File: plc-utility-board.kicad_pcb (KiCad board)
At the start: 2 copper layers, 116 parts, among them J1 Screw_Terminal_01x02, J10 Screw_Terminal_01x03, J11 Screw_Terminal_01x02, J12 Screw_Terminal_01x04, J2 Screw_Terminal_01x08, J3 Screw_Terminal_01x04, J4 Screw_Terminal_01x08, J5 Screw_Terminal_01x04, J6 Conn_01x03_Male, J7 Conn_01x03_Male, J8 Screw_Terminal_01x03, J9 Screw_Terminal_01x02, Q1 2N7002, Q10 2N7002, Q11 2N7002, Q12 2N7002, Q13 FDV304, Q14 2N7002, Q15 2N7002, Q16 2N7002, Q2 2N7002, Q3 Q_PMOS_GSD, Q4 Q_PMOS_GSD, Q5 2N7002, Q6 2N7002, Q7 Q_PMOS_GSD, Q8 Q_PMOS_GSD, Q9 FDV304, SW1 SW_Push, SW2 SW_Push, SW3 SW_Push, SW4 SW_Push, SW5 SW_Push, SW6 SW_Push, U1 L78L33_SOT89, U2 DRV8840, U3 DRV8840

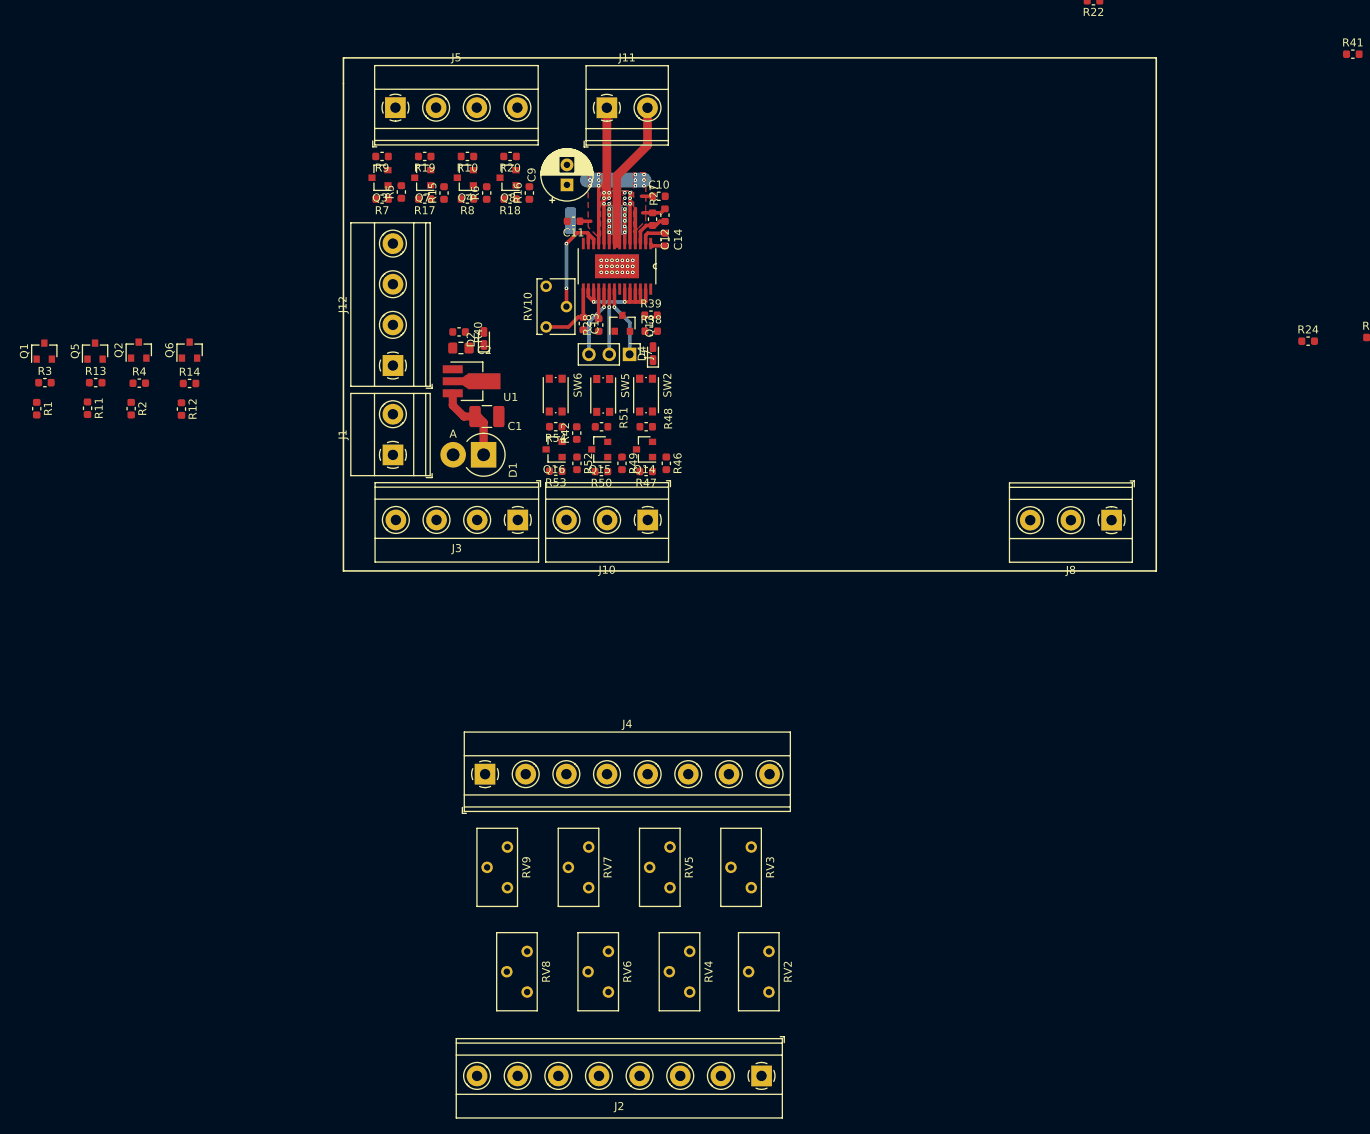
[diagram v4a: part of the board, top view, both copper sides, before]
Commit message: Re-placed components of 3.3->24V converter. Improvement placement of Motor Controller components
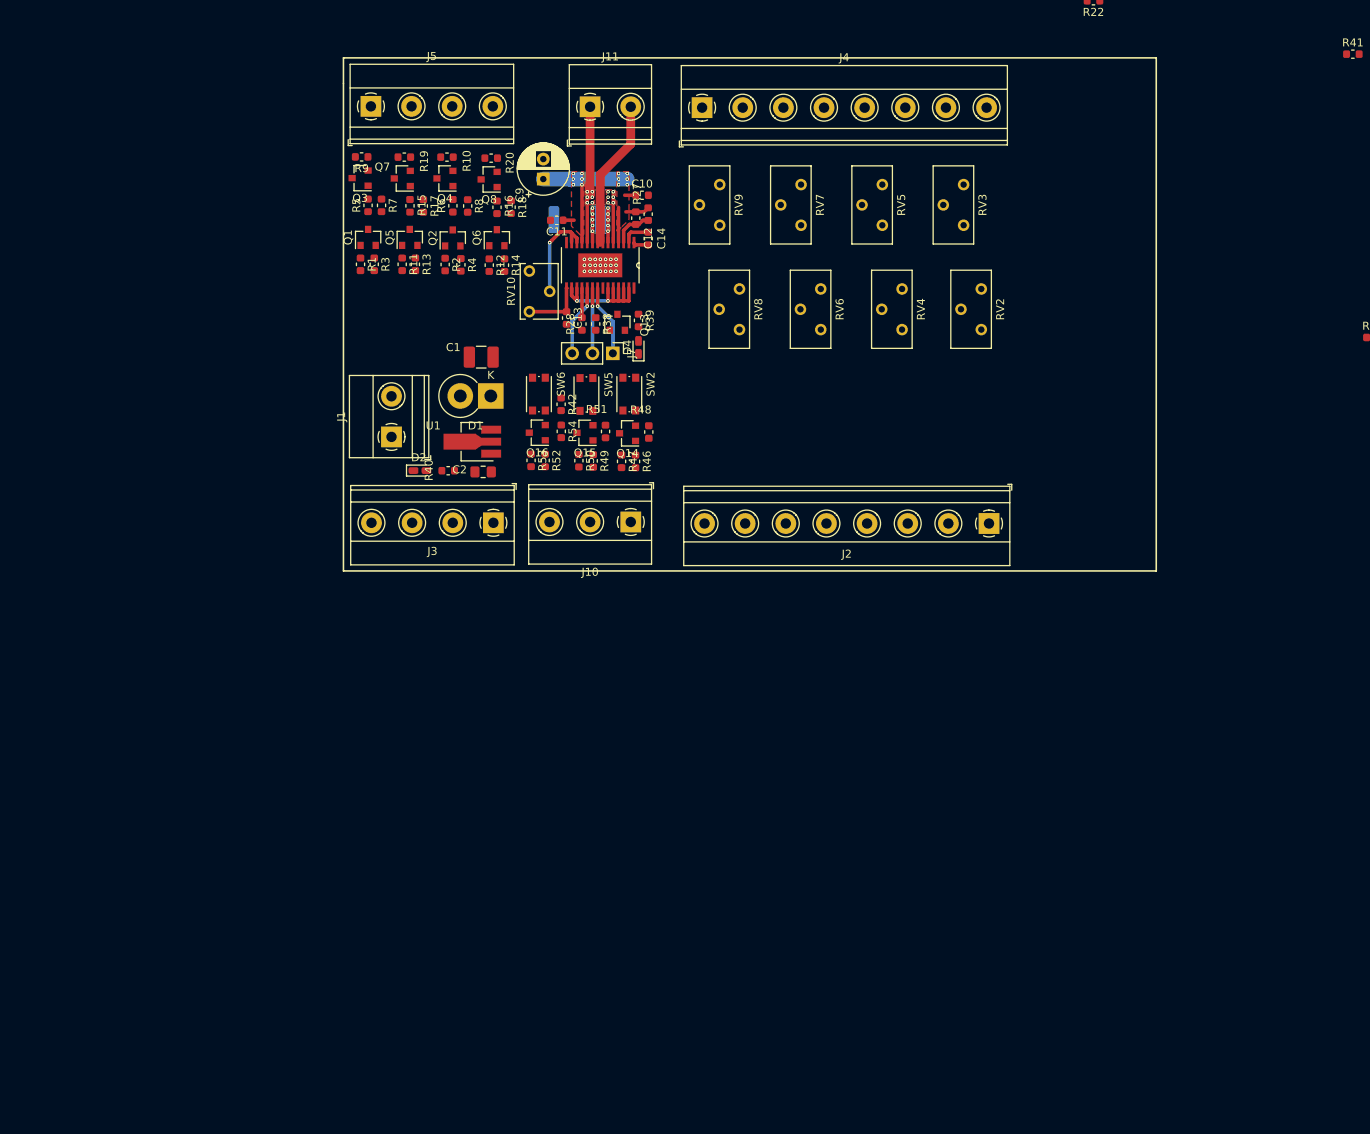
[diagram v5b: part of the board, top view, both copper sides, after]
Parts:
- removed J12: Screw_Terminal_01x04, TerminalBlock_Phoenix:TerminalBlock_Phoenix_MKDS-1,5-4-5.08_1x04_P5.08mm_Horizontal
- removed J8: Screw_Terminal_01x03, TerminalBlock_Phoenix:TerminalBlock_Phoenix_MKDS-1,5-3-5.08_1x03_P5.08mm_Horizontal
- removed R24: 10k, Resistor_SMD:R_0603_1608Metric
- D1: footprint Diode_THT:D_DO-201AD_P3.81mm_Vertical_AnodeUp -> Diode_THT:D_DO-201AD_P3.81mm_Vertical_KathodeUp
- moved J4 87.6 mm to (146.4, 69.1)
- moved RV3 87.0 mm to (179.1, 83.8)
- moved RV5 87.0 mm to (169.0, 83.8)
- moved RV7 87.0 mm to (158.8, 83.8)
- moved RV9 87.0 mm to (148.6, 83.8)
- moved RV2 87.0 mm to (181.3, 96.8)
- moved RV4 87.0 mm to (171.4, 96.8)
- moved RV6 87.0 mm to (161.3, 96.8)
- moved RV8 87.0 mm to (151.1, 96.8)
- moved J2 74.7 mm to (182.3, 121.1)
- moved R1 44.3 mm to (103.7, 88.7)
- moved R3 43.7 mm to (105.4, 88.7), turned to 270 degrees
- moved R11 43.2 mm to (108.9, 88.7)
- moved R2 43.2 mm to (114.3, 88.7)
- moved Q1 42.9 mm to (104.7, 85.3)
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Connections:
- J1 pad 1: /Power section/VIN -> GND
- J1 pad 2: GND -> /Power section/VIN
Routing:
- net /Power section/24V: track 34.8 -> 27.8 mm
- net Net-(RV10-Pad2): track 14.1 -> 12.3 mm, vias 2 -> 1
- net Net-(C13-Pad1): track 8.71 -> 7.62 mm

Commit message: Aligned references of components. Duplicated motor controller section
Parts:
- removed the J6 at (257.7, 72.6)
- added J6: Screw_Terminal_01x03, TerminalBlock_Phoenix:TerminalBlock_Phoenix_MKDS-1,5-3-5.08_1x03_P5.08mm_Horizontal, F.Cu at (237.5, 120.9)
- added J6: Conn_01x03_Male, Connector_PinHeader_2.54mm:PinHeader_1x03_P2.54mm_Vertical, F.Cu at (235.3, 100.2)
- added R24: 10k, Resistor_SMD:R_0603_1608Metric, F.Cu at (233.1, 96.1)
- R21: moved to B.Cu
- moved D3 122.9 mm to (238.5, 99.1), turned to 90 degrees
- moved R23 114.3 mm to (231.4, 96.1), turned to 90 degrees
- moved C8 109.7 mm to (239.7, 85.4), turned to 90 degrees
- moved U2 108.2 mm to (233.7, 88.8), turned to 270 degrees
- moved RV1 104.4 mm to (224.8, 89.5), turned to 90 degrees
- moved C3 100.8 mm to (226.6, 78.0), turned to 90 degrees
- moved R21 98.8 mm to (230.8, 83.1), turned to 180 degrees
- moved J9 79.0 mm to (232.4, 69.0)
- moved R31 67.0 mm to (239.8, 109.9)
- moved Q10 66.6 mm to (237.1, 110.1)
- moved R29 66.1 mm to (238.1, 113.6)
- moved R34 65.9 mm to (234.4, 109.9)
- moved R30 65.6 mm to (236.5, 113.6)
- moved Q11 65.5 mm to (231.8, 110.1)
- moved R32 65.0 mm to (232.8, 113.6)
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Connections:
- C6 pad 1: Net-(C6-Pad1) -> Net-(C12-Pad1)
- C7 pad 1: Net-(C7-Pad1) -> Net-(C13-Pad1)
- C8 pad 1: Net-(C8-Pad1) -> Net-(C14-Pad1)
- C8 pad 2: Net-(C8-Pad2) -> Net-(C14-Pad2)
- D3 pad 2: Net-(D3-Pad2) -> Net-(D4-Pad2)
- J9 pad 1: /Motor1 driver/OUT2 -> /Motor2 driver/OUT1
- J9 pad 2: /Motor1 driver/OUT1 -> /Motor2 driver/OUT2
- Q10 pad 1: Net-(Q10-Pad1) -> Net-(Q14-Pad1)
- Q10 pad 2: /Motor1 driver/ENABLE -> /Motor2 driver/ENABLE
- Q11 pad 1: Net-(Q11-Pad1) -> Net-(Q15-Pad1)
- Q11 pad 2: /Motor1 3V3 <- PLC/OUT2 -> /Motor2 3V3 <- PLC/OUT2
- Q12 pad 1: Net-(Q12-Pad1) -> Net-(Q16-Pad1)
- Q12 pad 2: /Motor1 driver/DECAY -> /Motor2 driver/DECAY
- Q9 pad 1: Net-(Q9-Pad1) -> Net-(Q13-Pad1)
- Q9 pad 3: Net-(Q9-Pad3) -> Net-(Q13-Pad3)
- R21 pad 1: Net-(R21-Pad1) -> Net-(R26-Pad1)
- R22 pad 1: Net-(C6-Pad1) -> Net-(C12-Pad1)
- R23 pad 1: Net-(Q9-Pad1) -> Net-(Q13-Pad1)
- R23 pad 2: Net-(R23-Pad2) -> Net-(R28-Pad2)
- R25 pad 1: Net-(Q9-Pad3) -> Net-(Q13-Pad3)
- R25 pad 2: Net-(D3-Pad2) -> Net-(D4-Pad2)
- R29 pad 1: Net-(Q10-Pad1) -> Net-(Q14-Pad1)
- R29 pad 2: /Motor1 3V3 <- PLC/IN1 -> /Motor2 3V3 <- PLC/IN1
- R30 pad 1: Net-(Q10-Pad1) -> Net-(Q14-Pad1)
- R31 pad 1: /Motor1 driver/ENABLE -> /Motor2 driver/ENABLE
- R32 pad 1: Net-(Q11-Pad1) -> Net-(Q15-Pad1)
- R32 pad 2: /Motor1 3V3 <- PLC/IN2 -> /Motor2 3V3 <- PLC/IN2
- R33 pad 1: Net-(Q11-Pad1) -> Net-(Q15-Pad1)
- R34 pad 1: /Motor1 3V3 <- PLC/OUT2 -> /Motor2 3V3 <- PLC/OUT2
- R35 pad 1: Net-(Q12-Pad1) -> Net-(Q16-Pad1)
- R35 pad 2: /Motor1 3V3 <- PLC/IN3 -> /Motor2 3V3 <- PLC/IN3
- R36 pad 1: Net-(Q12-Pad1) -> Net-(Q16-Pad1)
- R37 pad 1: /Motor1 driver/DECAY -> /Motor2 driver/DECAY
- R41 pad 2: /Motor1 driver/DECAY -> /Motor2 driver/DECAY
- RV1 pad 2: Net-(RV1-Pad2) -> Net-(RV10-Pad2)
- RV1 pad 3: Net-(C7-Pad1) -> Net-(C13-Pad1)
- SW1 pad 1: /Motor1 driver/ENABLE -> /Motor2 driver/ENABLE
- SW3 pad 1: /Motor1 3V3 <- PLC/OUT2 -> /Motor2 3V3 <- PLC/OUT2
- SW4 pad 1: /Motor1 driver/DECAY -> /Motor2 driver/DECAY
- U2 pad 1: Net-(C8-Pad1) -> Net-(C14-Pad1)
- U2 pad 10: /Motor1 driver/OUT1 -> /Motor2 driver/OUT1
- U2 pad 12: Net-(RV1-Pad2) -> Net-(RV10-Pad2)
- U2 pad 13: Net-(RV1-Pad2) -> Net-(RV10-Pad2)
- U2 pad 15: Net-(C7-Pad1) -> Net-(C13-Pad1)
- U2 pad 18: Net-(R23-Pad2) -> Net-(R28-Pad2)
- U2 pad 19: /Motor1 driver/DECAY -> /Motor2 driver/DECAY
- U2 pad 2: Net-(C8-Pad2) -> Net-(C14-Pad2)
- U2 pad 20: /Motor1 3V3 <- PLC/OUT2 -> /Motor2 3V3 <- PLC/OUT2
- U2 pad 21: /Motor1 driver/ENABLE -> /Motor2 driver/ENABLE
- U2 pad 22: Net-(U2-Pad22) -> Net-(U3-Pad22)
- U2 pad 3: Net-(C6-Pad1) -> Net-(C12-Pad1)
- U2 pad 5: /Motor1 driver/OUT1 -> /Motor2 driver/OUT1
- U2 pad 6: Net-(R21-Pad1) -> Net-(R26-Pad1)
- U2 pad 7: /Motor1 driver/OUT2 -> /Motor2 driver/OUT2
- U2 pad 8: /Motor1 driver/OUT2 -> /Motor2 driver/OUT2
- U2 pad 9: Net-(R21-Pad1) -> Net-(R26-Pad1)
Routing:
- net /Power section/24V: track 27.8 -> 55.7 mm, vias 12 -> 24
- net /Motor2 driver/OUT1: track 23.8 -> 47.5 mm, vias 12 -> 24
- net /Motor1 3V3 <- PLC/3V3: track 18.9 -> 37.8 mm, vias 2 -> 4
- net /Motor2 driver/OUT2: track 18.6 -> 37.1 mm
- net Net-(RV10-Pad2): track 12.3 -> 24.7 mm, vias 1 -> 2
- net /Motor2 driver/DECAY: track 9.17 -> 18.3 mm, vias 1 -> 2
- net /Motor2 driver/ENABLE: track 8.97 -> 17.9 mm, vias 1 -> 2
- net Net-(R26-Pad1): track 8.59 -> 17.2 mm, vias 10 -> 20
- net /Motor2 3V3 <- PLC/OUT2: track 8.40 -> 16.8 mm, vias 1 -> 2
- net Net-(C13-Pad1): track 7.62 -> 15.2 mm
- net Net-(C12-Pad1): track 5.12 -> 10.2 mm
- net Net-(R28-Pad2): track 3.59 -> 7.17 mm
- net Net-(C14-Pad2): track 3.55 -> 7.10 mm
- net Net-(C14-Pad1): track 1.95 -> 3.90 mm
- net GND: vias 21 -> 42

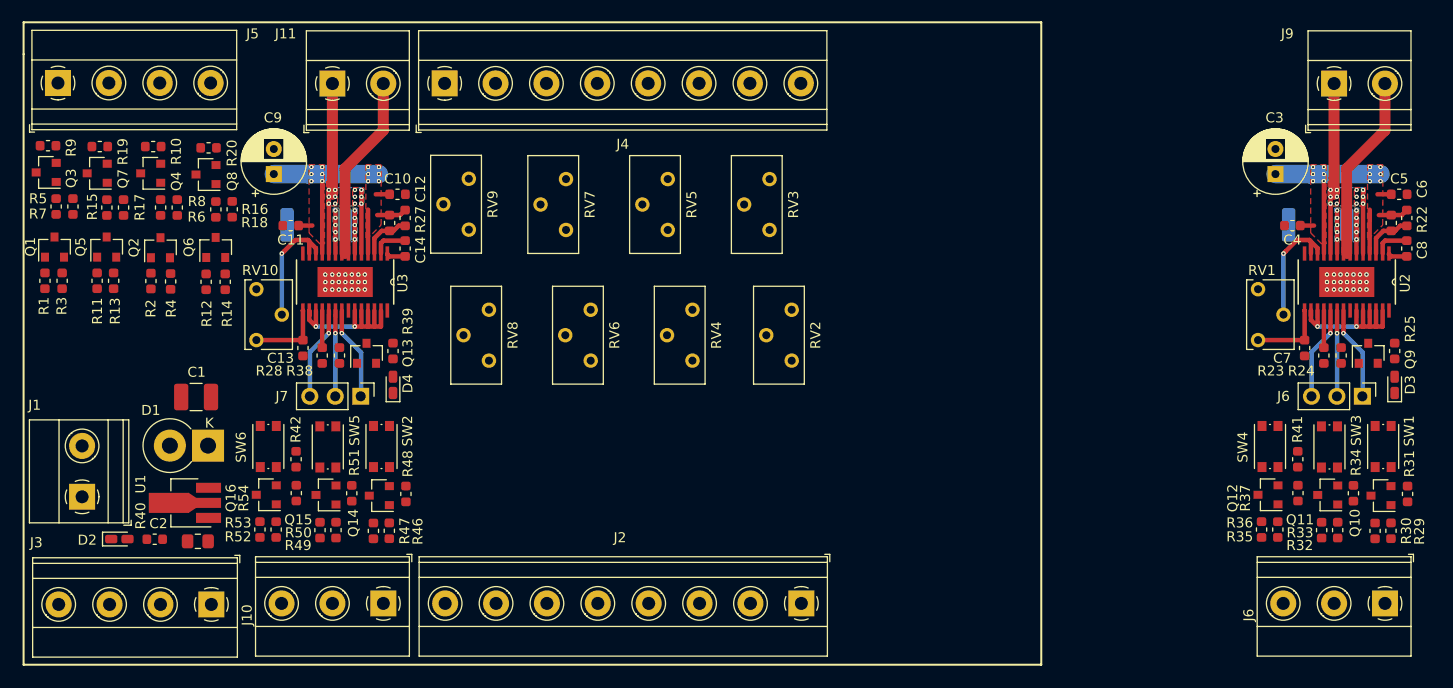
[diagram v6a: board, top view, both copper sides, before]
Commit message: Routed all nets without GND. Added logo
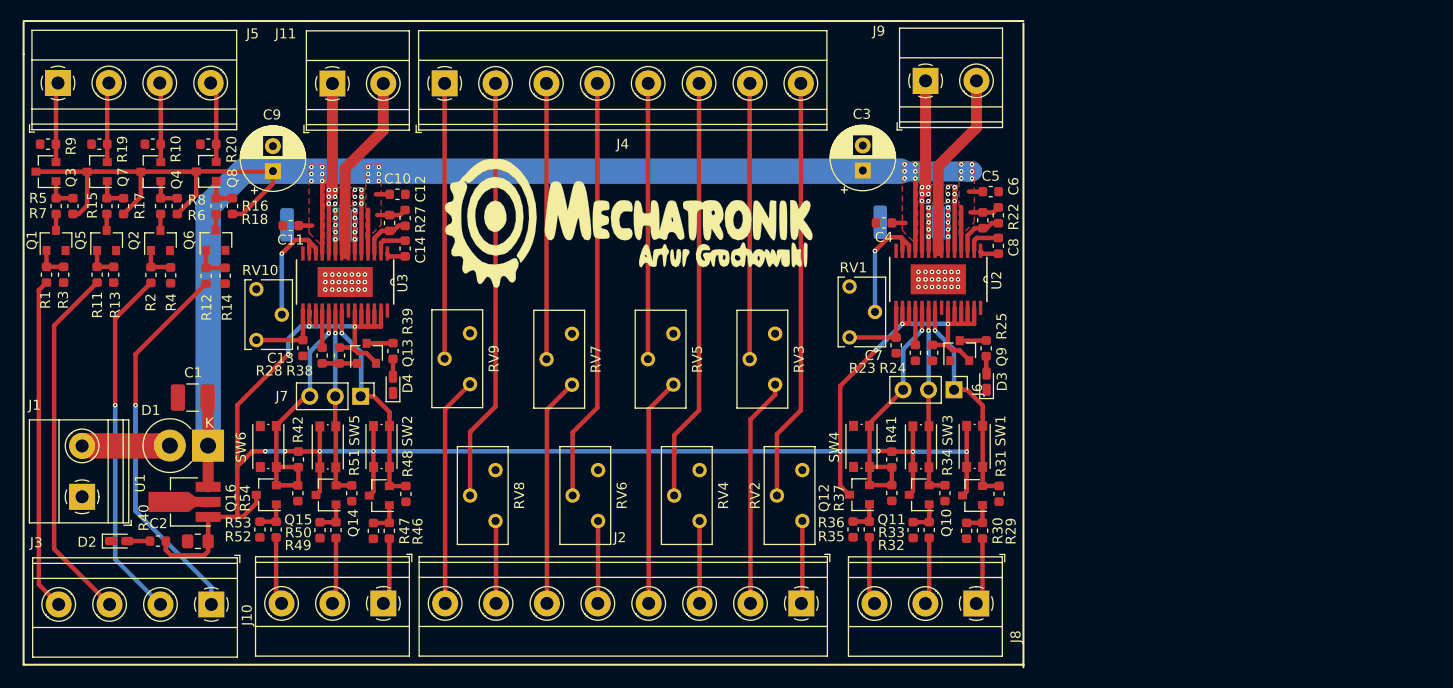
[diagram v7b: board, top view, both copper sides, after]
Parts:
- removed the J6 at (237.5, 120.9)
- removed the J6 at (235.3, 100.2)
- added G***: LOGO, plc-utility-board:logo, F.Cu at (145.3, 77.7)
- added G***: LOGO, plc-utility-board:logo, F.Cu at (161.9, 82.8)
- added J6: Conn_01x03_Male, Connector_PinHeader_2.54mm:PinHeader_1x03_P2.54mm_Vertical, F.Cu at (194.5, 99.6)
- added J8: Screw_Terminal_01x03, TerminalBlock_Phoenix:TerminalBlock_Phoenix_MKDS-1,5-3-5.08_1x03_P5.08mm_Horizontal, F.Cu at (196.7, 120.9)
- moved C3 41.2 mm to (185.4, 77.7)
- moved C4 40.8 mm to (187.5, 82.9)
- moved C5 40.8 mm to (198.2, 79.8)
- moved C6 40.8 mm to (198.9, 82.1)
- moved J9 40.8 mm to (191.7, 68.7)
- moved RV1 40.8 mm to (184.1, 89.2)
- moved C7 40.8 mm to (188.7, 95.1)
- moved C8 40.8 mm to (198.9, 85.2)
- moved Q9 40.8 mm to (195.1, 95.6)
- moved R21 40.8 mm to (190.0, 82.8)
- moved R22 40.8 mm to (197.4, 82.6)
- moved R23 40.8 mm to (190.6, 95.9)
- moved R24 40.8 mm to (192.4, 95.9)
- moved R25 40.8 mm to (197.7, 95.4)
- moved U2 40.8 mm to (192.9, 88.5)
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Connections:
- C6 pad 1: Net-(C12-Pad1) -> Net-(C6-Pad1)
- C7 pad 1: Net-(C13-Pad1) -> Net-(C7-Pad1)
- C8 pad 1: Net-(C14-Pad1) -> Net-(C8-Pad1)
- C8 pad 2: Net-(C14-Pad2) -> Net-(C8-Pad2)
- D3 pad 2: Net-(D4-Pad2) -> Net-(D3-Pad2)
- J9 pad 1: /Motor2 driver/OUT1 -> /Motor1 driver/OUT1
- J9 pad 2: /Motor2 driver/OUT2 -> /Motor1 driver/OUT2
- Q10 pad 1: Net-(Q14-Pad1) -> Net-(Q10-Pad1)
- Q10 pad 2: /Motor2 driver/ENABLE -> /Motor1 driver/ENABLE
- Q11 pad 1: Net-(Q15-Pad1) -> Net-(Q11-Pad1)
- Q11 pad 2: /Motor2 3V3 <- PLC/OUT2 -> /Motor1 3V3 <- PLC/OUT2
- Q12 pad 1: Net-(Q16-Pad1) -> Net-(Q12-Pad1)
- Q12 pad 2: /Motor2 driver/DECAY -> /Motor1 driver/DECAY
- Q9 pad 1: Net-(Q13-Pad1) -> Net-(Q9-Pad1)
- Q9 pad 3: Net-(Q13-Pad3) -> Net-(Q9-Pad3)
- R21 pad 1: Net-(R26-Pad1) -> Net-(R21-Pad1)
- R22 pad 1: Net-(C12-Pad1) -> Net-(C6-Pad1)
- R23 pad 1: Net-(Q13-Pad1) -> Net-(Q9-Pad1)
- R23 pad 2: Net-(R28-Pad2) -> Net-(R23-Pad2)
- R24 pad 2: Net-(Q13-Pad1) -> Net-(Q9-Pad1)
- R25 pad 1: Net-(Q13-Pad3) -> Net-(Q9-Pad3)
- R25 pad 2: Net-(D4-Pad2) -> Net-(D3-Pad2)
- R29 pad 1: Net-(Q14-Pad1) -> Net-(Q10-Pad1)
- R29 pad 2: /Motor2 3V3 <- PLC/IN1 -> /Motor1 3V3 <- PLC/IN1
- R30 pad 1: Net-(Q14-Pad1) -> Net-(Q10-Pad1)
- R31 pad 1: /Motor2 driver/ENABLE -> /Motor1 driver/ENABLE
- R32 pad 1: Net-(Q15-Pad1) -> Net-(Q11-Pad1)
- R32 pad 2: /Motor2 3V3 <- PLC/IN2 -> /Motor1 3V3 <- PLC/IN2
- R33 pad 1: Net-(Q15-Pad1) -> Net-(Q11-Pad1)
- R34 pad 1: /Motor2 3V3 <- PLC/OUT2 -> /Motor1 3V3 <- PLC/OUT2
- R35 pad 1: Net-(Q16-Pad1) -> Net-(Q12-Pad1)
- R35 pad 2: /Motor2 3V3 <- PLC/IN3 -> /Motor1 3V3 <- PLC/IN3
- R36 pad 1: Net-(Q16-Pad1) -> Net-(Q12-Pad1)
- R37 pad 1: /Motor2 driver/DECAY -> /Motor1 driver/DECAY
- R41 pad 2: /Motor2 driver/DECAY -> /Motor1 driver/DECAY
- RV1 pad 2: Net-(RV10-Pad2) -> Net-(RV1-Pad2)
- RV1 pad 3: Net-(C13-Pad1) -> Net-(C7-Pad1)
- SW1 pad 1: /Motor2 driver/ENABLE -> /Motor1 driver/ENABLE
- SW3 pad 1: /Motor2 3V3 <- PLC/OUT2 -> /Motor1 3V3 <- PLC/OUT2
- SW4 pad 1: /Motor2 driver/DECAY -> /Motor1 driver/DECAY
- U2 pad 1: Net-(C14-Pad1) -> Net-(C8-Pad1)
- U2 pad 10: /Motor2 driver/OUT1 -> /Motor1 driver/OUT1
- U2 pad 12: Net-(RV10-Pad2) -> Net-(RV1-Pad2)
- U2 pad 13: Net-(RV10-Pad2) -> Net-(RV1-Pad2)
- U2 pad 15: Net-(C13-Pad1) -> Net-(C7-Pad1)
- U2 pad 18: Net-(R28-Pad2) -> Net-(R23-Pad2)
- U2 pad 19: /Motor2 driver/DECAY -> /Motor1 driver/DECAY
- U2 pad 2: Net-(C14-Pad2) -> Net-(C8-Pad2)
- U2 pad 20: /Motor2 3V3 <- PLC/OUT2 -> /Motor1 3V3 <- PLC/OUT2
- U2 pad 21: /Motor2 driver/ENABLE -> /Motor1 driver/ENABLE
- U2 pad 22: Net-(U3-Pad22) -> Net-(U2-Pad22)
- U2 pad 3: Net-(C12-Pad1) -> Net-(C6-Pad1)
- U2 pad 5: /Motor2 driver/OUT1 -> /Motor1 driver/OUT1
- U2 pad 6: Net-(R26-Pad1) -> Net-(R21-Pad1)
- U2 pad 7: /Motor2 driver/OUT2 -> /Motor1 driver/OUT2
- U2 pad 8: /Motor2 driver/OUT2 -> /Motor1 driver/OUT2
- U2 pad 9: Net-(R26-Pad1) -> Net-(R21-Pad1)
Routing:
- net /Motor1 3V3 <- PLC/3V3: track 37.8 -> 210.6 mm, vias 4 -> 14
- net /Power section/24V: track 55.7 -> 191.1 mm
- net /plc-to-ttl/OUT2: track 0.00 -> 42.2 mm
- net /plc-to-ttl/OUT6: track 0.00 -> 42.2 mm
- net /plc-to-ttl/OUT4: track 0.00 -> 42.2 mm
- net /plc-to-ttl/OUT8: track 0.00 -> 42.1 mm
- net /ttl-to-plc/IN4: track 0.00 -> 38.1 mm, vias 0 -> 1
- net /ttl-to-plc/IN2: track 0.00 -> 36.2 mm
- net /ttl-to-plc/IN3: track 0.00 -> 35.5 mm, vias 0 -> 1
- net /ttl-to-plc/IN1: track 0.00 -> 33.3 mm
- net /plc-to-ttl/OUT3: track 0.00 -> 27.5 mm
- net /plc-to-ttl/OUT7: track 0.00 -> 27.5 mm
- net /plc-to-ttl/OUT5: track 0.00 -> 27.5 mm
- net /plc-to-ttl/OUT1: track 0.00 -> 27.5 mm
- net /Motor1 driver/DECAY: track 0.00 -> 26.1 mm, vias 0 -> 1
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- added copper zone on B.Cu, net /Motor1 driver/OUT1
- added copper zone on F.Cu, net /Motor1 driver/OUT1
- added copper zone on B.Cu, net Net-(R21-Pad1)
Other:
- net class Default: clearance 0.1 -> 0.175
- rule trace_clearance: 0.1 -> 0.175
